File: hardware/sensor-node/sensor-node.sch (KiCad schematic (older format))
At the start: 51 parts, among them J1 CONUFL001-SMD-T, J2 SHF-105-01-L-D-TH, Q1 PMV250EPEA, U1 TLV61225, U2 TPS27081A, U3 SHT31-DIS, U4 24LC32, U5 MLX90614, U6 ADG633YRU, U7 TSV911RILT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

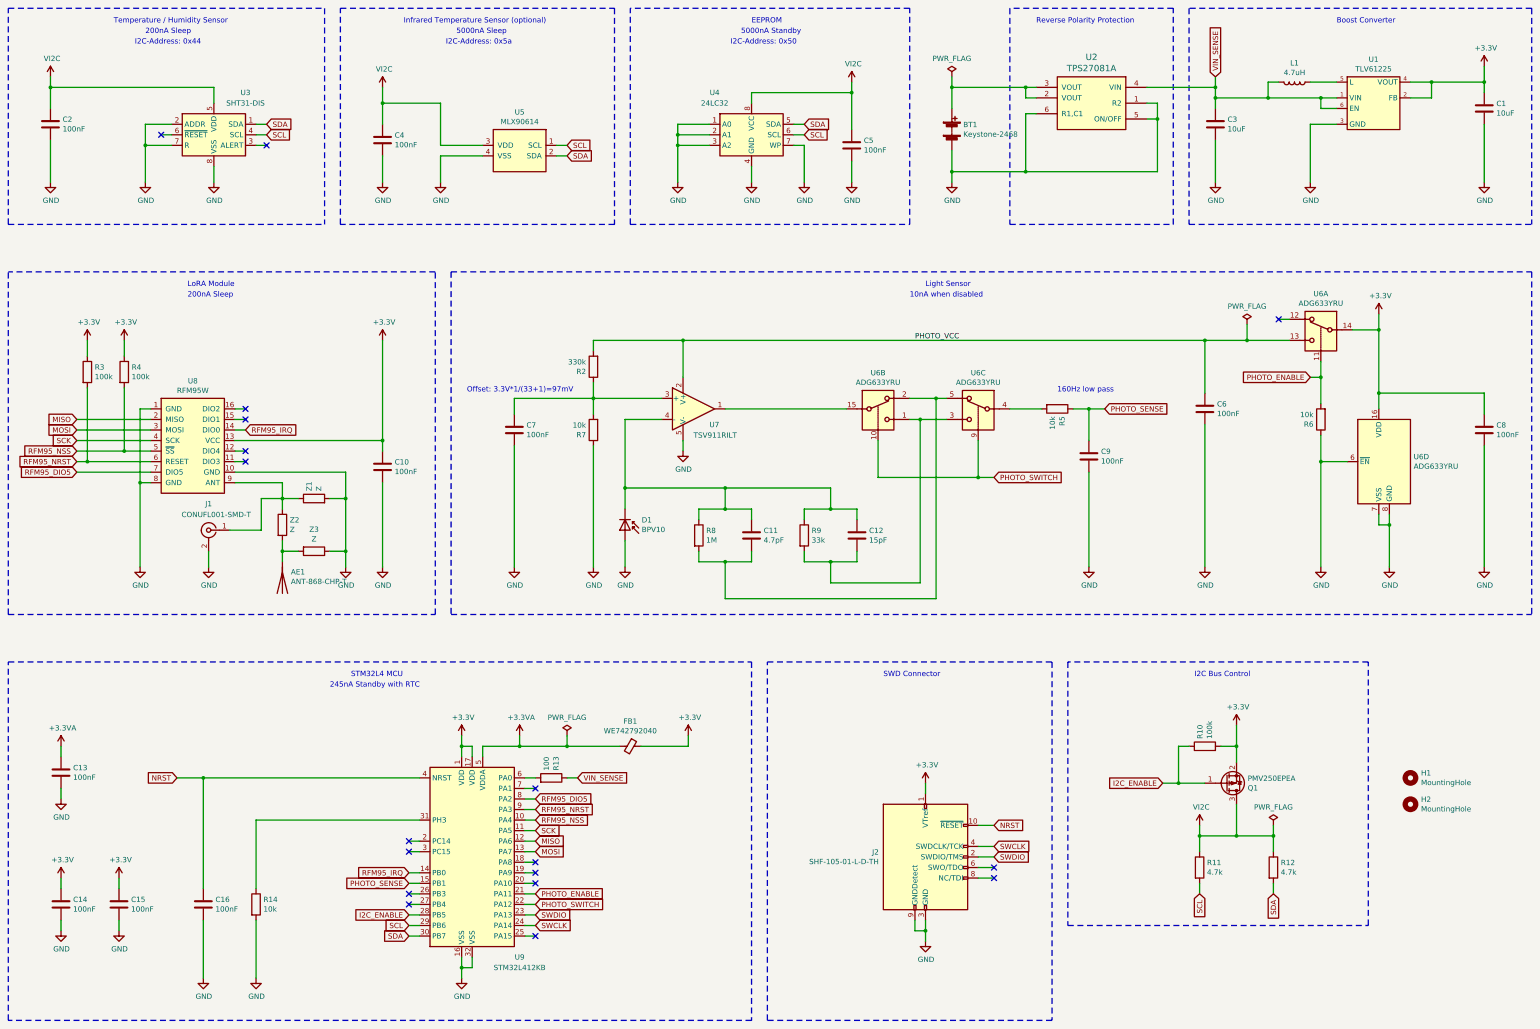
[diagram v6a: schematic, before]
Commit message: Fix PCB problems for Rev. 2
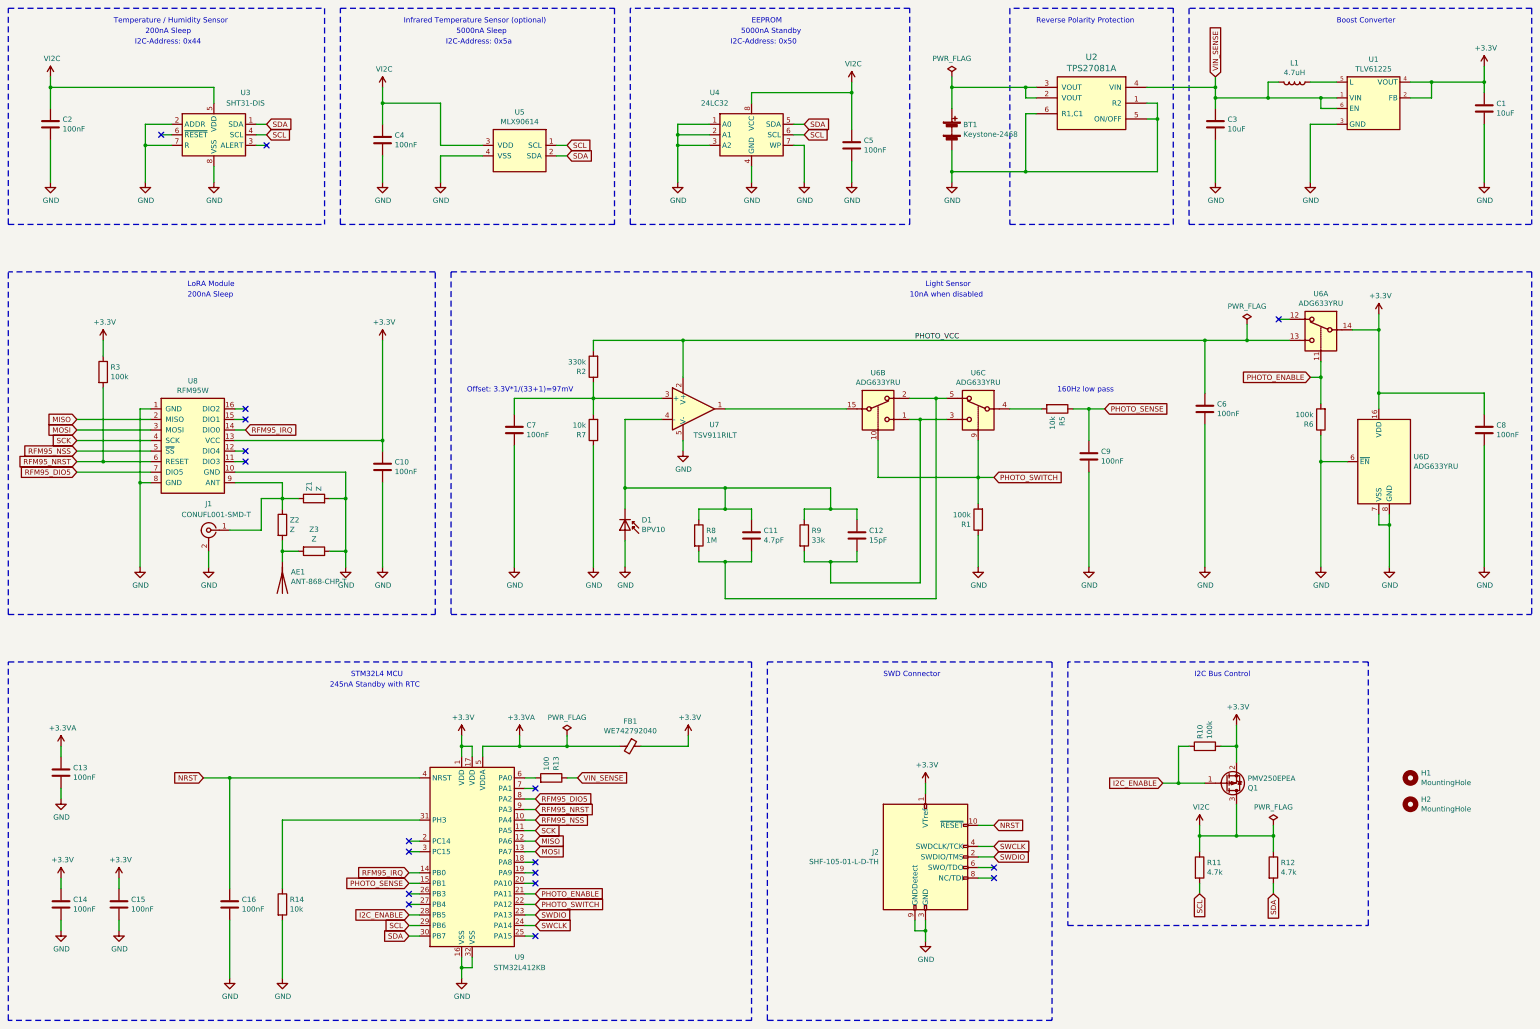
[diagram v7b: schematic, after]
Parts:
- removed R4: 100k, Resistor_SMD:R_0805_2012Metric_Pad1.20x1.40mm_HandSolder, symbol Device:R
- added R1: 100k, Resistor_SMD:R_0805_2012Metric_Pad1.20x1.40mm_HandSolder, symbol Device:R
- FB1: footprint Inductor_SMD:L_0805_2012Metric_Pad1.05x1.20mm_HandSolder -> Inductor_SMD:L_0805_2012Metric_Pad1.15x1.40mm_HandSolder
- R6: value 10k -> 100k
- U1: footprint Package_TO_SOT_SMD:TSOT-23-6 -> my-footprints-library:SC-70-6
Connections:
- net GND: now also R1.1
- net PHOTO_SWITCH: now also R1.2
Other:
- moved on the sheet: C16, R14, R3
